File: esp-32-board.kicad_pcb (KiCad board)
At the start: 2 copper layers, 53.8 x 69.1 mm, 39 parts, among them J1 USB_B_Micro, J2 Conn_Arduino_UNO_R3, J3 Conn_02x03_Odd_Even, J4 ESP-PROG-Program, J5 ESP-PROG-Debug, J6 Barrel_Jack_MountingPin, Q1 2N2219, Q2 2N2219, Q3 AO3401A, SW1 SW_Push, SW2 SW_Push, SW3 SW_SPST, U1 AMS1117-3.3, U2 CP2102N-A01-GQFN28, U3 ESP32-WROOM-32, U4 MC33269DT−5.0, U5 LM358, U6 USBLC6-2SC6

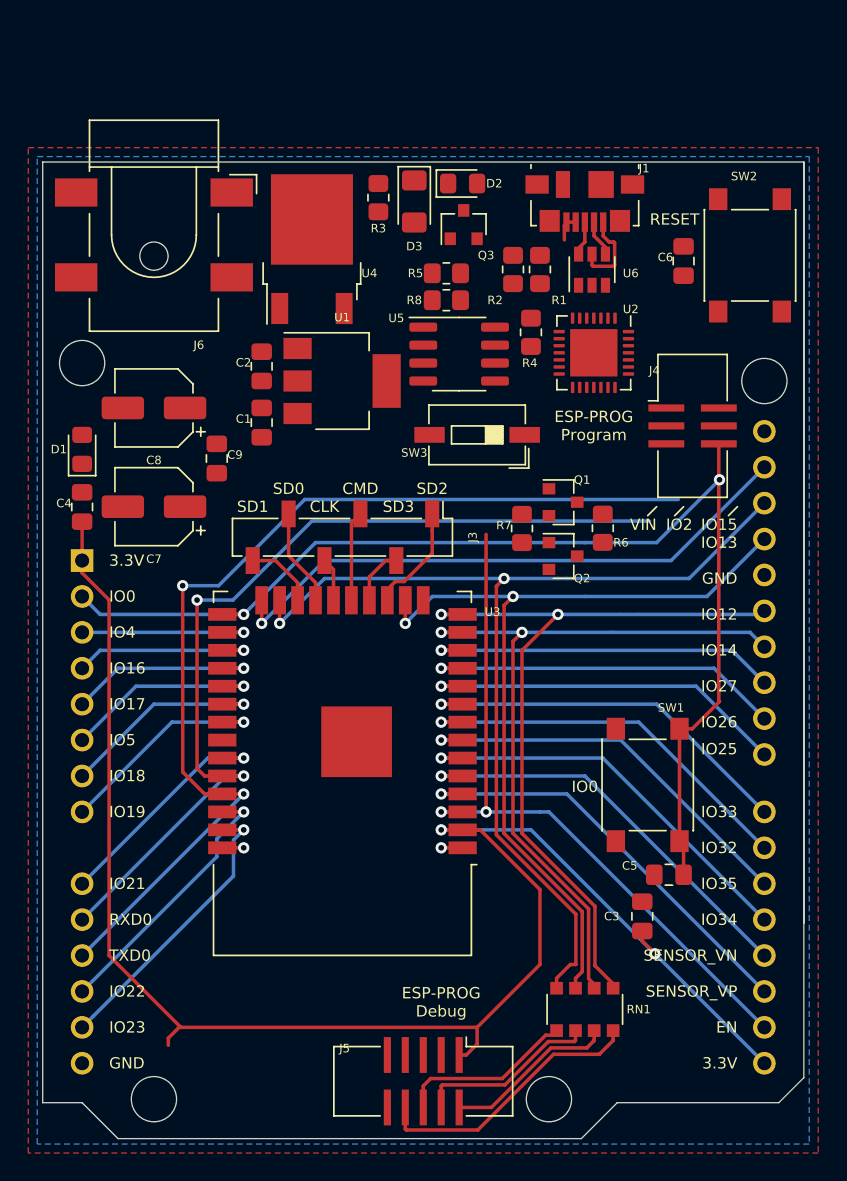
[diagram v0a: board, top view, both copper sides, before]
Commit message: Reorganize symbols & update vendors
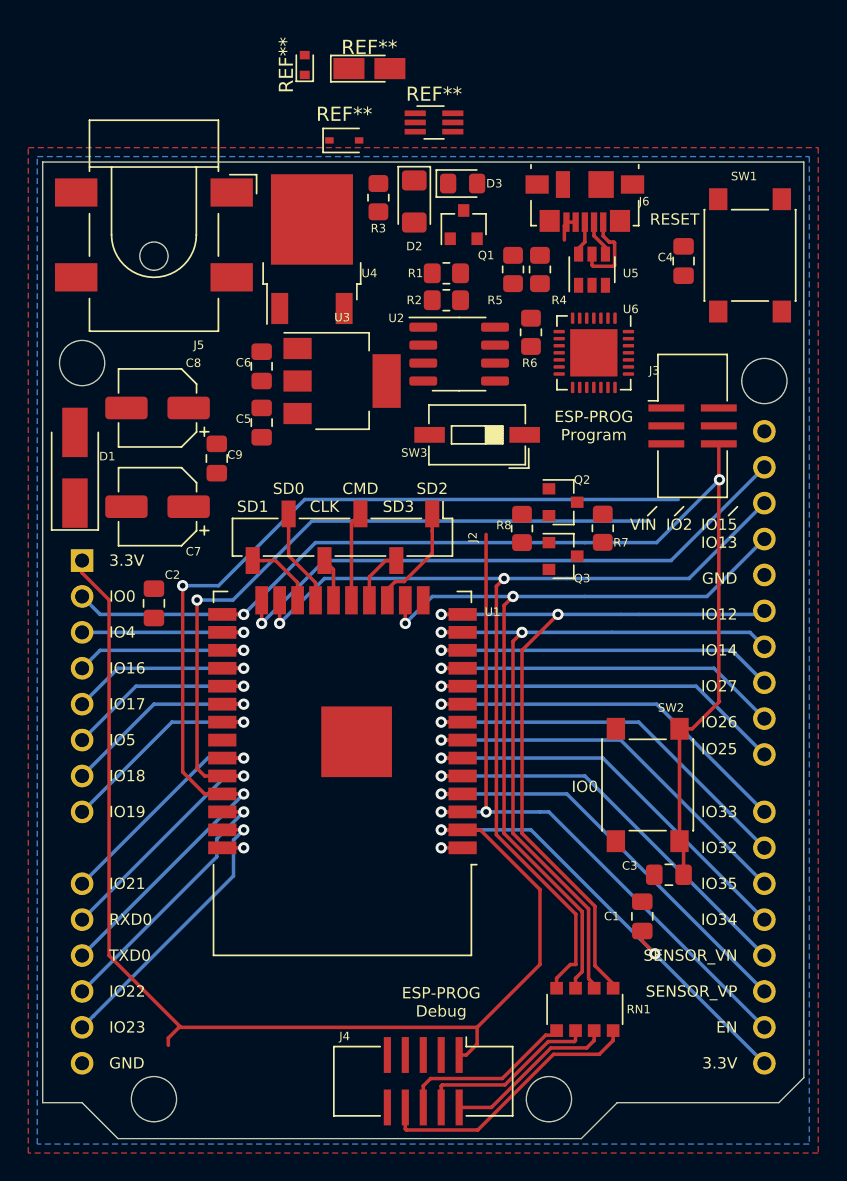
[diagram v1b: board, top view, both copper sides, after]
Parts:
- removed the J2 at (132.1, 49.5)
- removed the U3 at (150.5, 61.6)
- added J1: Conn_Arduino_UNO_R3, Module:Arduino_UNO_R3_WithMountingHoles, B.Cu at (132.1, 49.5)
- added REF**: D_SOD-323, Diode_SMD:D_SOD-323, F.Cu at (150.6, 19.8)
- added REF**: SOT-363_SC-70-6_Handsoldering, Package_TO_SOT_SMD:SOT-363_SC-70-6_Handsoldering, F.Cu at (157.0, 18.5)
- added REF**: D_MicroMELF_Handsoldering, Diode_SMD:D_MicroMELF_Handsoldering, F.Cu at (152.4, 14.7)
- added REF**: D_SOD-523, Diode_SMD:D_SOD-523, F.Cu at (147.8, 14.5)
- added U1: ESP32-WROOM-32, RF_Module:ESP32-WROOM-32, F.Cu at (150.5, 61.6)
- C1: renamed from C3; value C -> 4.7uF
- C2: renamed from C4; value C -> 100nF
- C3: renamed from C5; value C -> 100nF
- C4: renamed from C6; value C -> 100nF
- C5: renamed from C1; value C -> 22uF
- C6: renamed from C2; value C -> 22uF
- C7, C8: value CP -> 47uF
- C9: value C -> 100nF
- D1: value D -> M7; footprint Diode_SMD:D_0805_2012Metric_Pad1.15x1.40mm_HandSolder -> Diode_SMD:D_SMA_Handsoldering
- moved C2 8.50 mm to (137.2, 52.6), turned to 270 degrees
- moved D1 1.40 mm to (131.6, 43.0)
- moved C7 0.25 mm to (137.4, 45.7)
- moved C8 0.25 mm to (137.4, 38.7)
- renumbered D3 to D2, D2 to D3, J3 to J2, J4 to J3, J5 to J4, J6 to J5, J1 to J6, Q3 to Q1, Q1 to Q2, Q2 to Q3, R5 to R1, R8 to R2, R1 to R4, R2 to R5, R4 to R6, R6 to R7, R7 to R8, SW2 to SW1, SW1 to SW2, U5 to U2, U1 to U3, U6 to U5, U2 to U6
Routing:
- net +3V3: track 116.1 -> 113.4 mm
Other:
- outline, holes or cut-outs redrawn

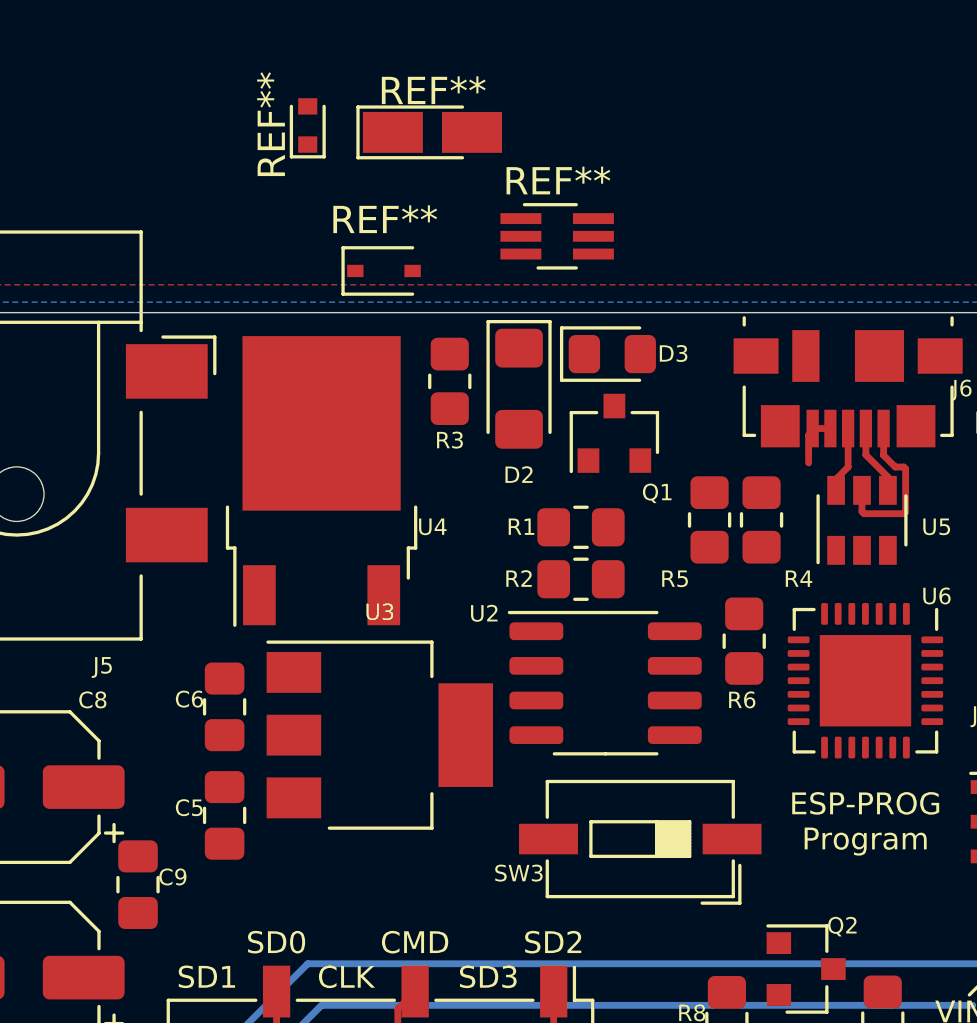
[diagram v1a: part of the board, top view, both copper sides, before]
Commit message: Remove Op-Amp circuit for USB power
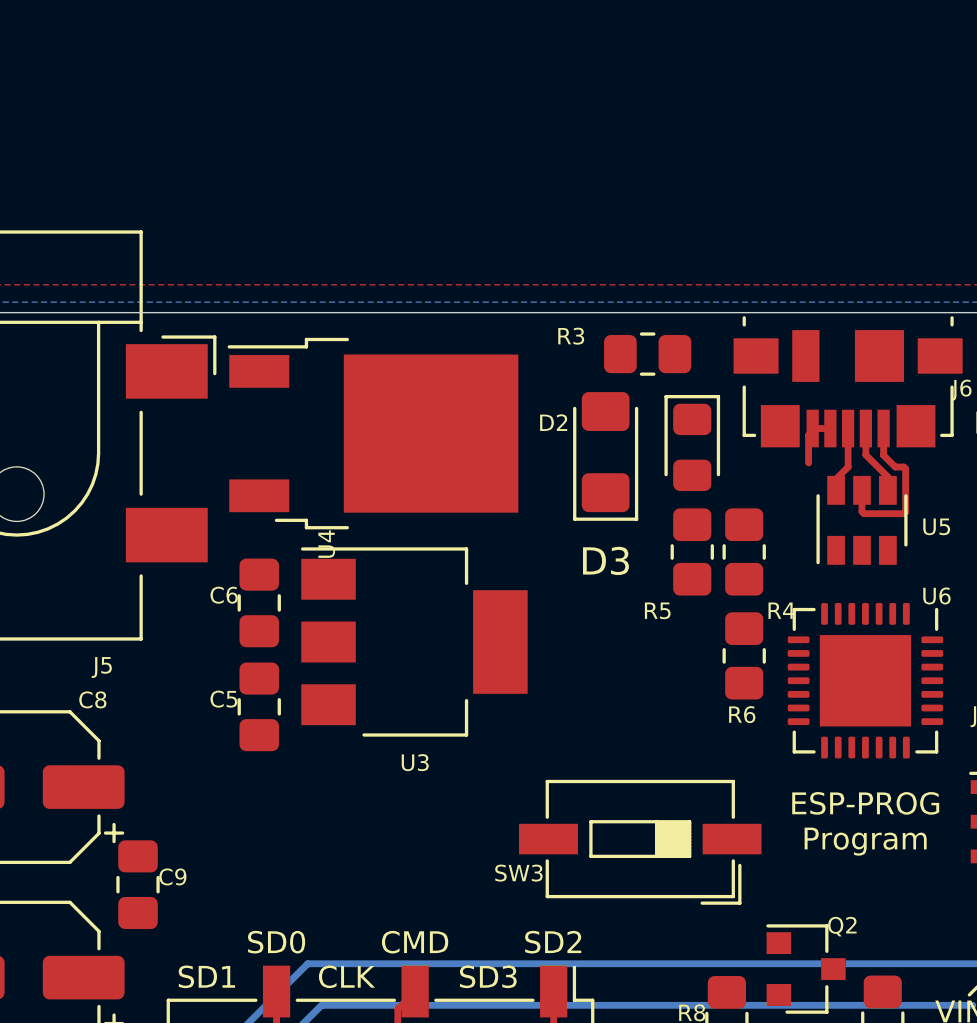
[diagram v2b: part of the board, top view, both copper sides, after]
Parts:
- removed Q1: AO3401A, Package_TO_SOT_SMD:SOT-23
- removed R1, R2: 10k Ohm, Resistor_SMD:R_0805_2012Metric_Pad1.20x1.40mm_HandSolder
- removed REF**: D_SOD-323, Diode_SMD:D_SOD-323
- removed REF**: SOT-363_SC-70-6_Handsoldering, Package_TO_SOT_SMD:SOT-363_SC-70-6_Handsoldering
- removed REF**: D_MicroMELF_Handsoldering, Diode_SMD:D_MicroMELF_Handsoldering
- removed REF**: D_SOD-523, Diode_SMD:D_SOD-523
- removed U2: LM358, Package_SO:SOP-8_3.76x4.96mm_P1.27mm
- D2: value LED -> RF-GSS150TS-BC
- D3: value D_Schottky -> STPS0520Z
- Q2, Q3: value 2N2219 -> ?
- R3: value ? Ohm -> 220 Ohm
- R4: value 22.1 Ohm -> 22k Ohm
- R5: value 47.5 Ohm -> 47k Ohm
- R6: value 2k Ohm -> 2.2k Ohm
- moved R3 7.32 mm to (160.3, 22.9), turned to 180 degrees
- moved D3 4.50 mm to (161.9, 26.3), turned to 270 degrees
- moved C5 4.18 mm to (146.1, 35.8)
- moved C6 4.02 mm to (146.1, 32.0)
- moved D2 3.93 mm to (158.8, 26.5), turned to 90 degrees
- moved U3 3.64 mm to (151.7, 33.4)
- moved U4 2.58 mm to (150.2, 25.8), turned to 0 degrees
- moved R4 1.34 mm to (163.8, 30.1)
- moved R5 1.34 mm to (161.9, 30.1)
- moved R6 0.54 mm to (163.8, 33.9)
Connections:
- net VBUS renamed /USB/VBUS
- D3 pad 1: Net-(D3-Pad1) -> +5V

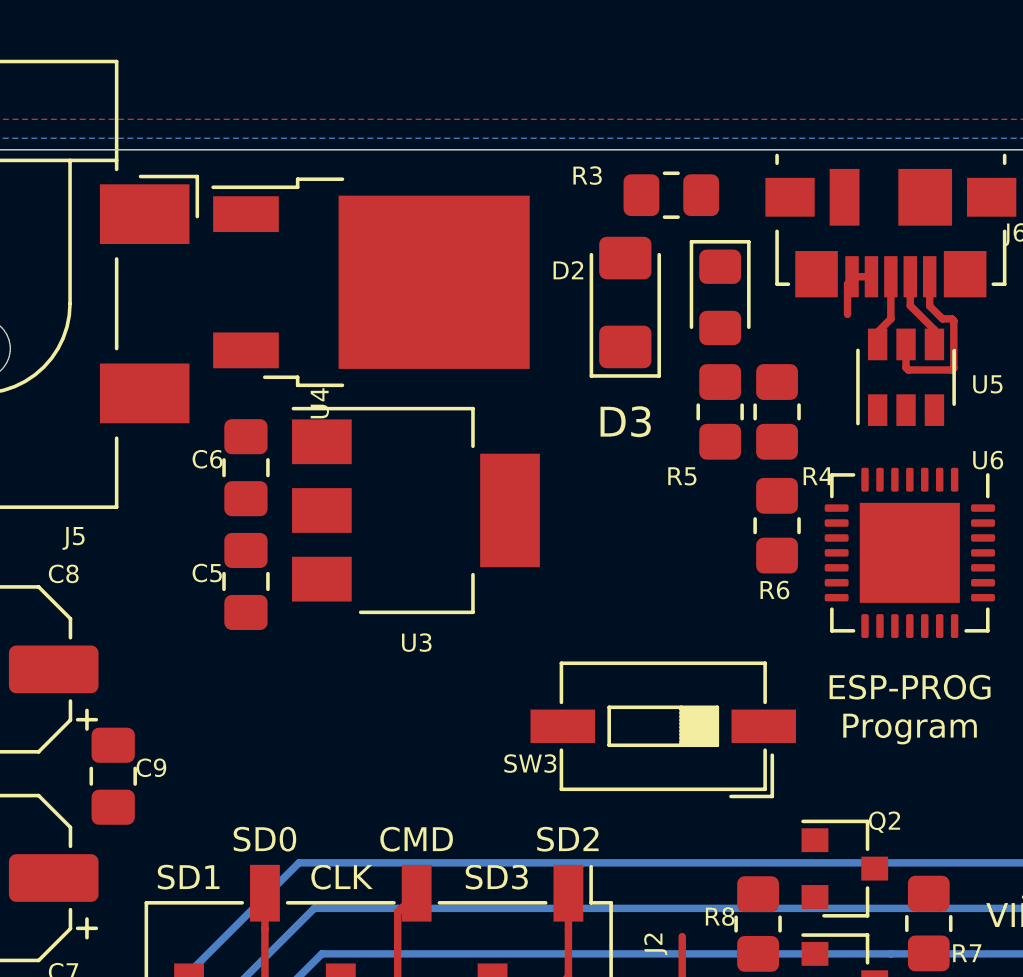
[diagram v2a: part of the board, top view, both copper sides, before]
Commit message: Change footprint of D3
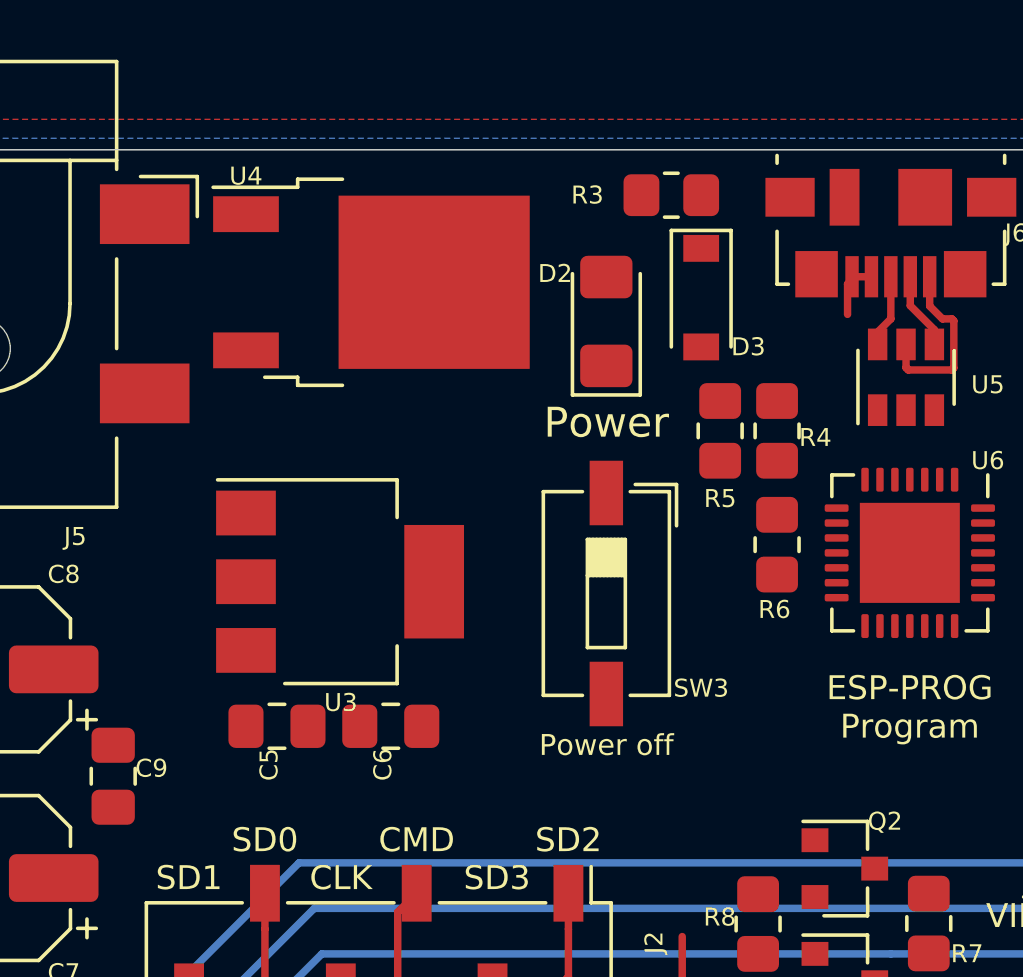
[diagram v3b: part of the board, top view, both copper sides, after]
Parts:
- D3: footprint Diode_SMD:D_0805_2012Metric_Pad1.15x1.40mm_HandSolder -> Diode_SMD:D_SOD-123
- moved C6 9.92 mm to (150.9, 40.6), turned to 180 degrees
- moved C5 4.96 mm to (147.1, 40.6), turned to 0 degrees
- moved SW3 4.84 mm to (158.1, 36.2), turned to 270 degrees
- moved U3 3.48 mm to (149.2, 35.8)
- moved D2 0.90 mm to (158.1, 27.1)
- moved D3 0.64 mm to (161.3, 26.3)
- moved R6 0.64 mm to (163.8, 34.6)
- moved R4 0.64 mm to (163.8, 30.8)
- moved R5 0.64 mm to (161.9, 30.8)
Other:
- board text added: "Power"
- board text added: "Power off"

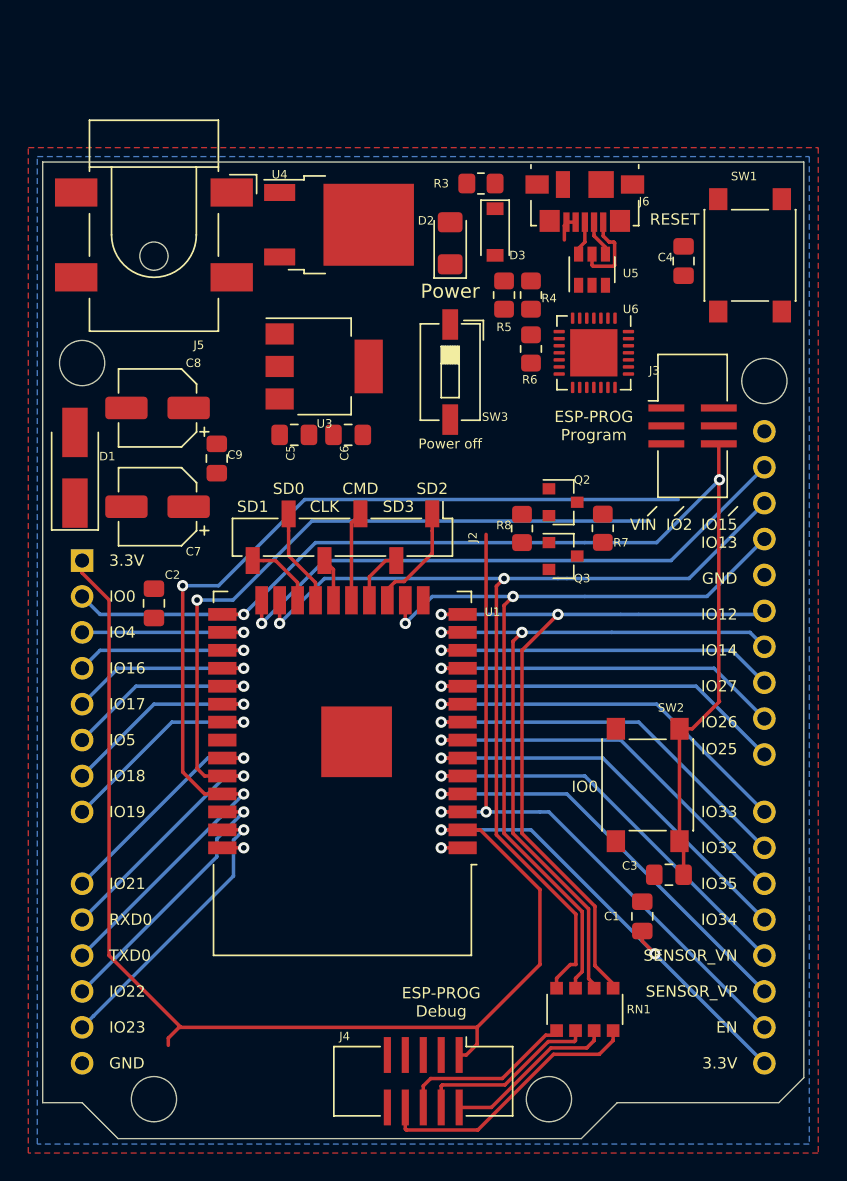
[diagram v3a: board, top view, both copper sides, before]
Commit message: Change regulators to NCP1117ST50T3G/NCP1117-3.3
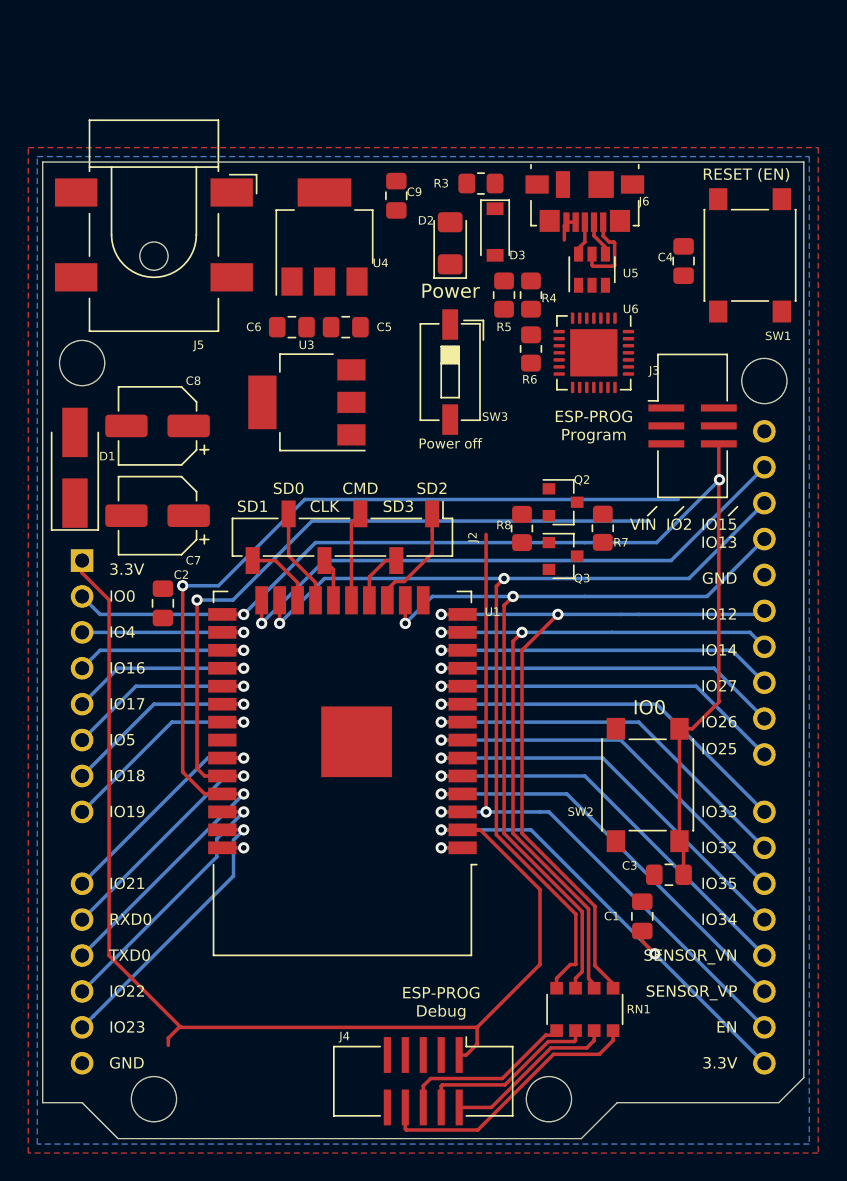
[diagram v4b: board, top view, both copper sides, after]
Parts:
- U3: value AMS1117-3.3 -> NCP1117-3.3
- U4: value MC33269DT−5.0 -> NCP1117ST50T3G; footprint Package_TO_SOT_SMD:TO-252-2 -> Package_TO_SOT_SMD:SOT-223-3_TabPin2
- moved C9 22.5 mm to (154.3, 23.7)
- moved C6 8.60 mm to (146.9, 33.0), turned to 0 degrees
- moved C5 8.44 mm to (150.7, 33.0), turned to 180 degrees
- moved U3 2.82 mm to (148.0, 38.3), turned to 180 degrees
- moved U4 1.34 mm to (149.2, 26.6), turned to 90 degrees
- moved C8 1.27 mm to (137.4, 40.0)
- moved C7 0.63 mm to (137.4, 46.4)
- moved C2 0.63 mm to (137.8, 52.6)
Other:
- board text added: "RESET (EN)"
- board text removed: "RESET"
